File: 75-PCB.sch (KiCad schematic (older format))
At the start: 12 parts

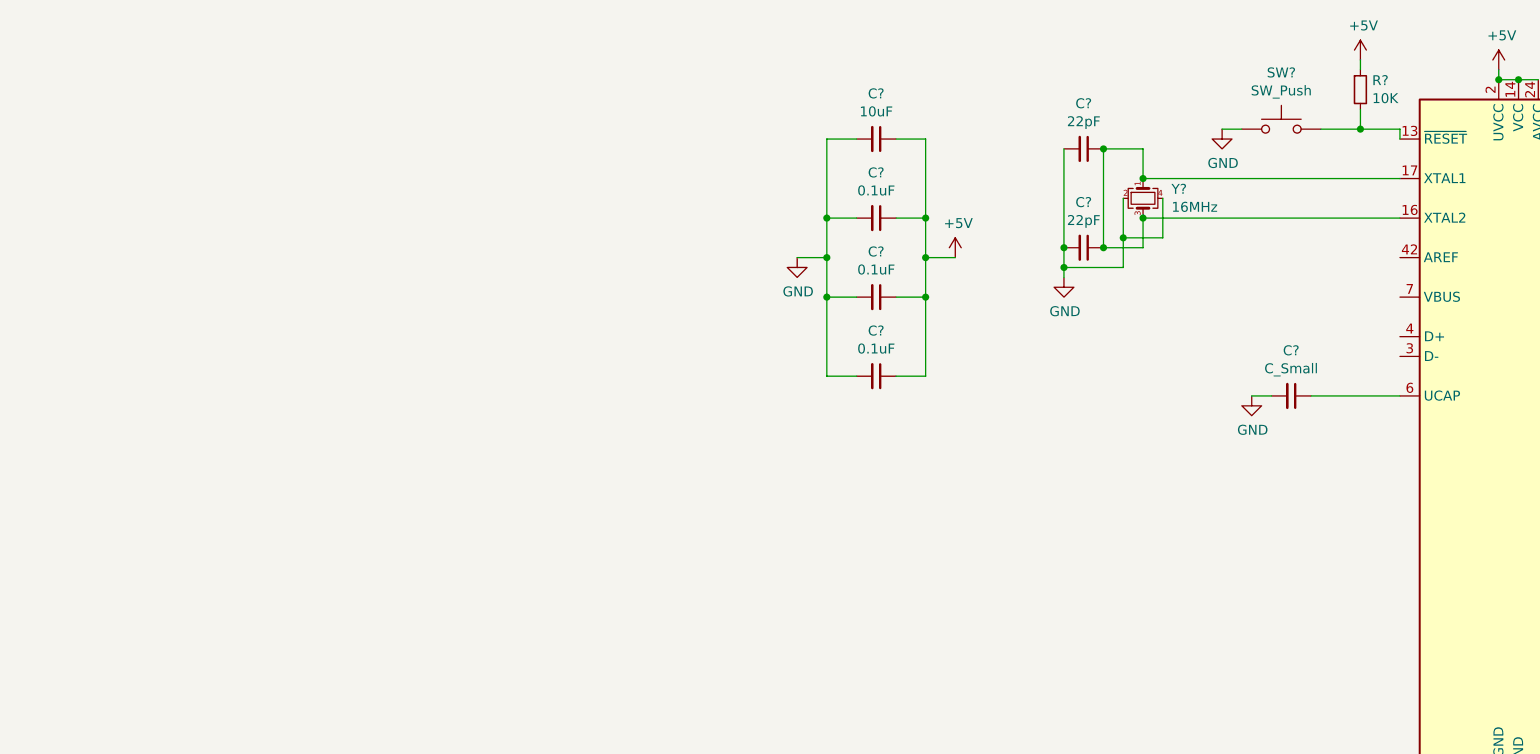
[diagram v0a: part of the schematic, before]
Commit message: Finished USB schematic
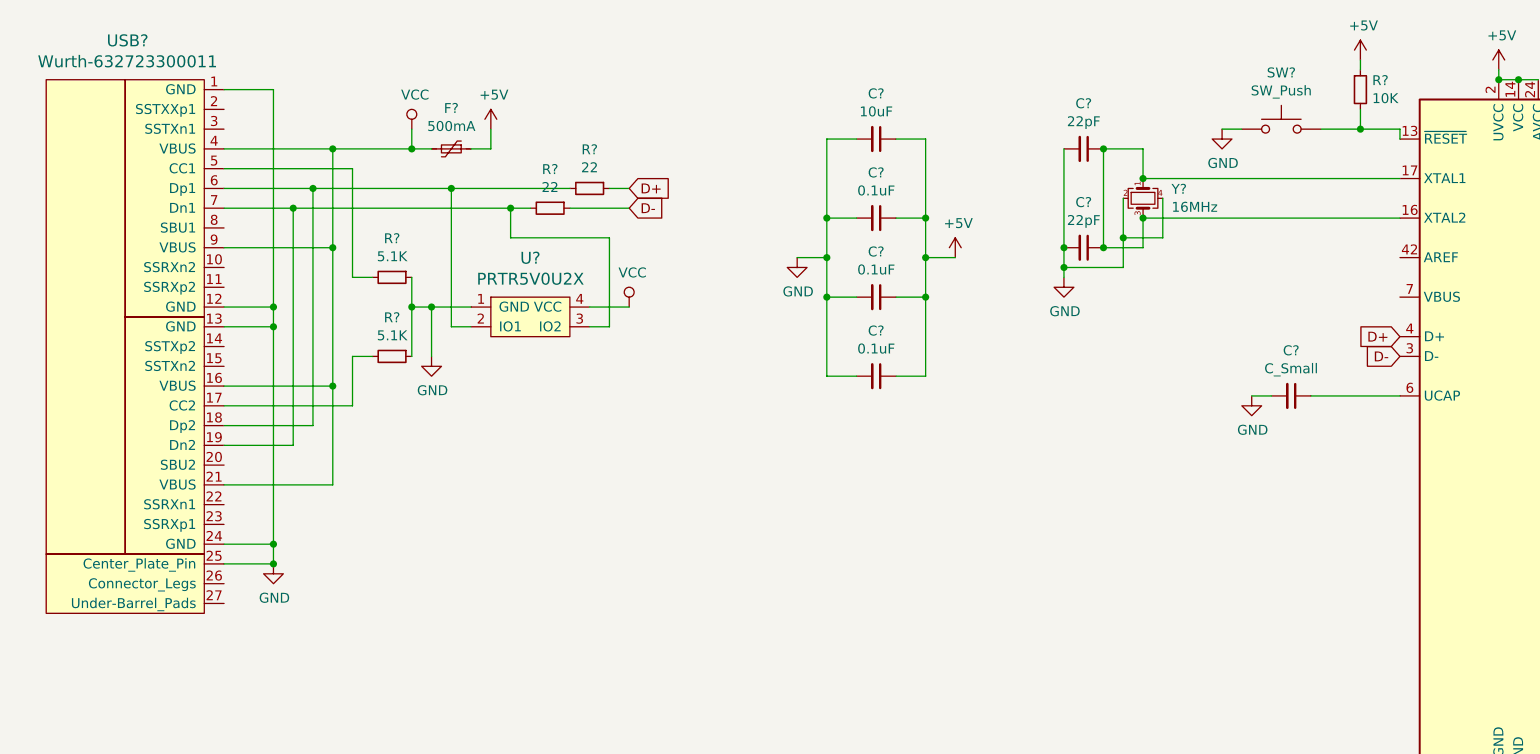
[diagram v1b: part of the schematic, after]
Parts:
- added F?: 500mA, symbol Device:Polyfuse_Small
- added R? (x2): 22, symbol Device:R_Small
- added R? (x2): 5.1K, symbol Device:R_Small
- added U?: PRTR5V0U2X, symbol random-keyboard-parts:PRTR5V0U2X
- added USB?: Wurth-632723300011, symbol Type-C:Wurth-632723300011
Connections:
- net +5V: now also F?.1
- net GND: now also R?.1, R?.1, U?.1 (GND), USB?.1 (GND), USB?.12 (GND), USB?.13 (GND), USB?.24 (GND), USB?.25 (Center_Plate_Pin)
- net D-: now reaches U?.3 (D-)
- net D-: now also R?.1
- net D+: now reaches U?.4 (D+)
- net D+: now also R?.1
- new net: R?.2, USB?.17 (CC2)
- new net: R?.2, U?.2 (IO1), USB?.18 (Dp2), USB?.6 (Dp1)
- new net: R?.2, U?.3 (IO2), USB?.19 (Dn2), USB?.7 (Dn1)
- new net: R?.2, USB?.5 (CC1)
- new net VCC: F?.2, U?.4 (VCC), USB?.16 (VBUS), USB?.21 (VBUS), USB?.4 (VBUS), USB?.9 (VBUS)

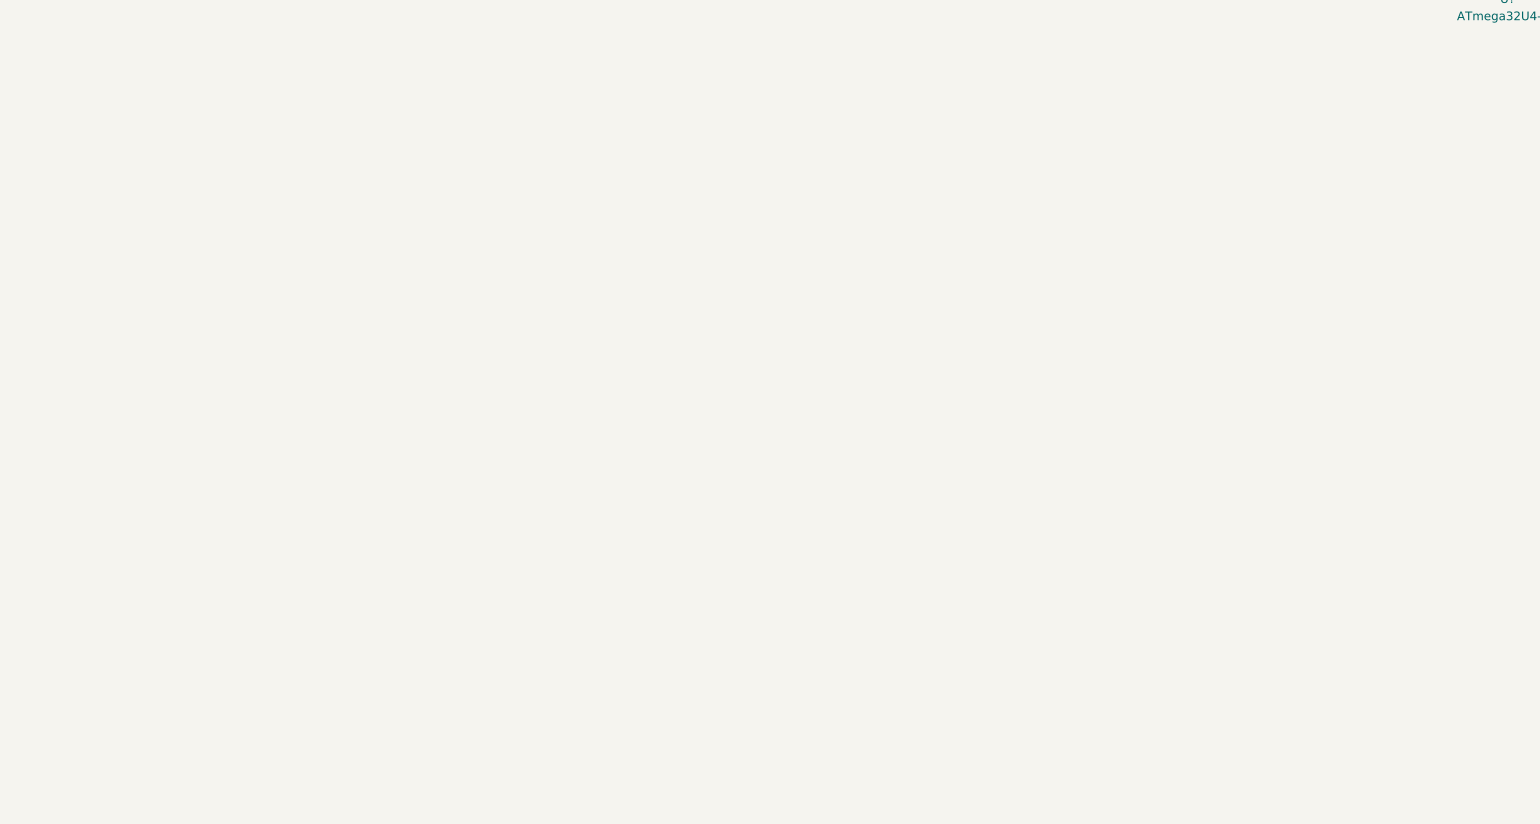
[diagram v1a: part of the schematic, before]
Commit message: Finished placing switch symbols
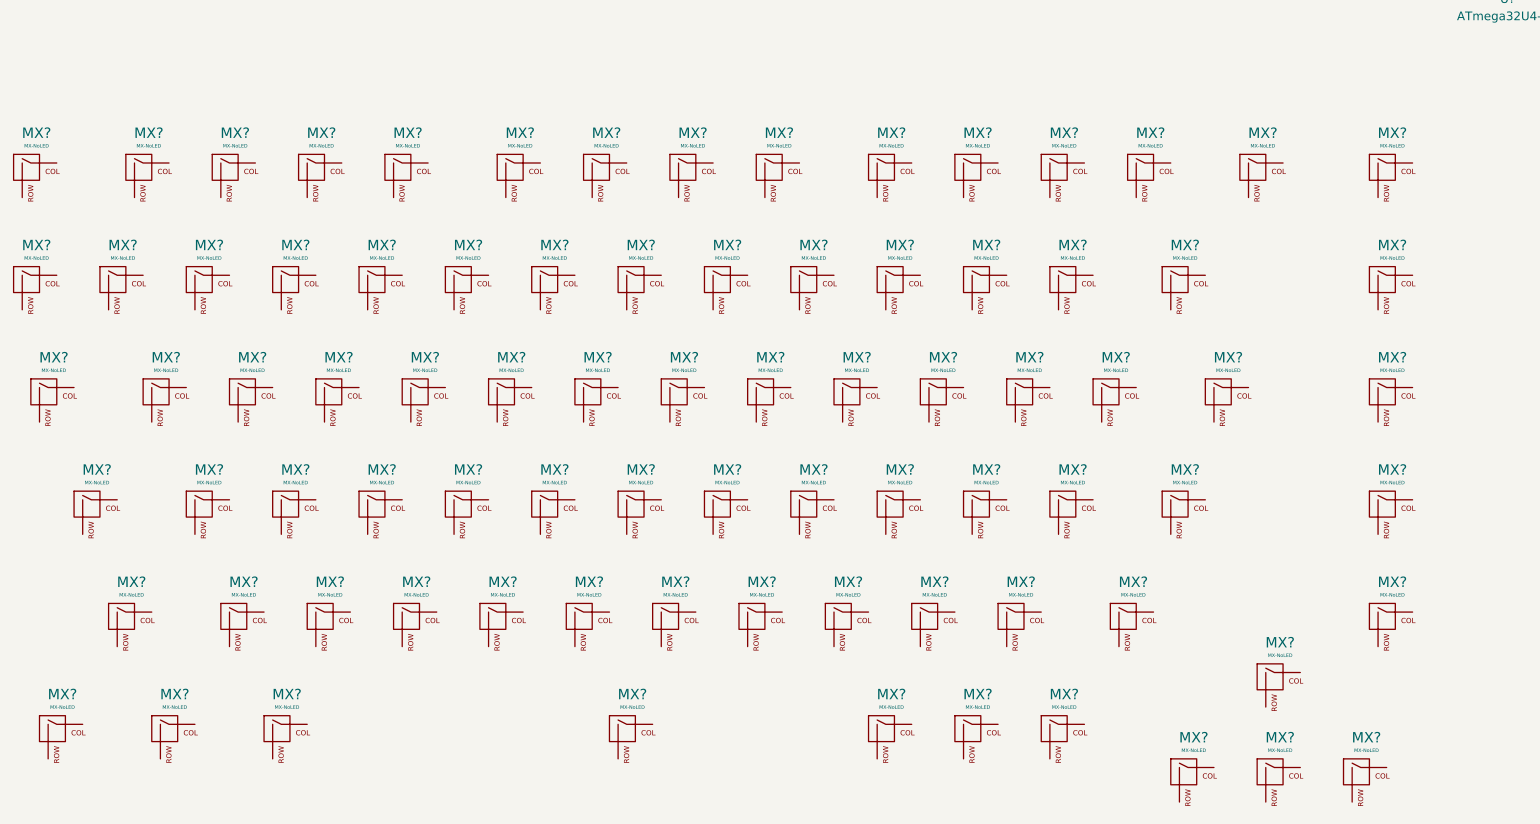
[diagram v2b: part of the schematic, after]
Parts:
- added MX? (x83): MX-NoLED, symbol MX_Alps_Hybrid:MX-NoLED

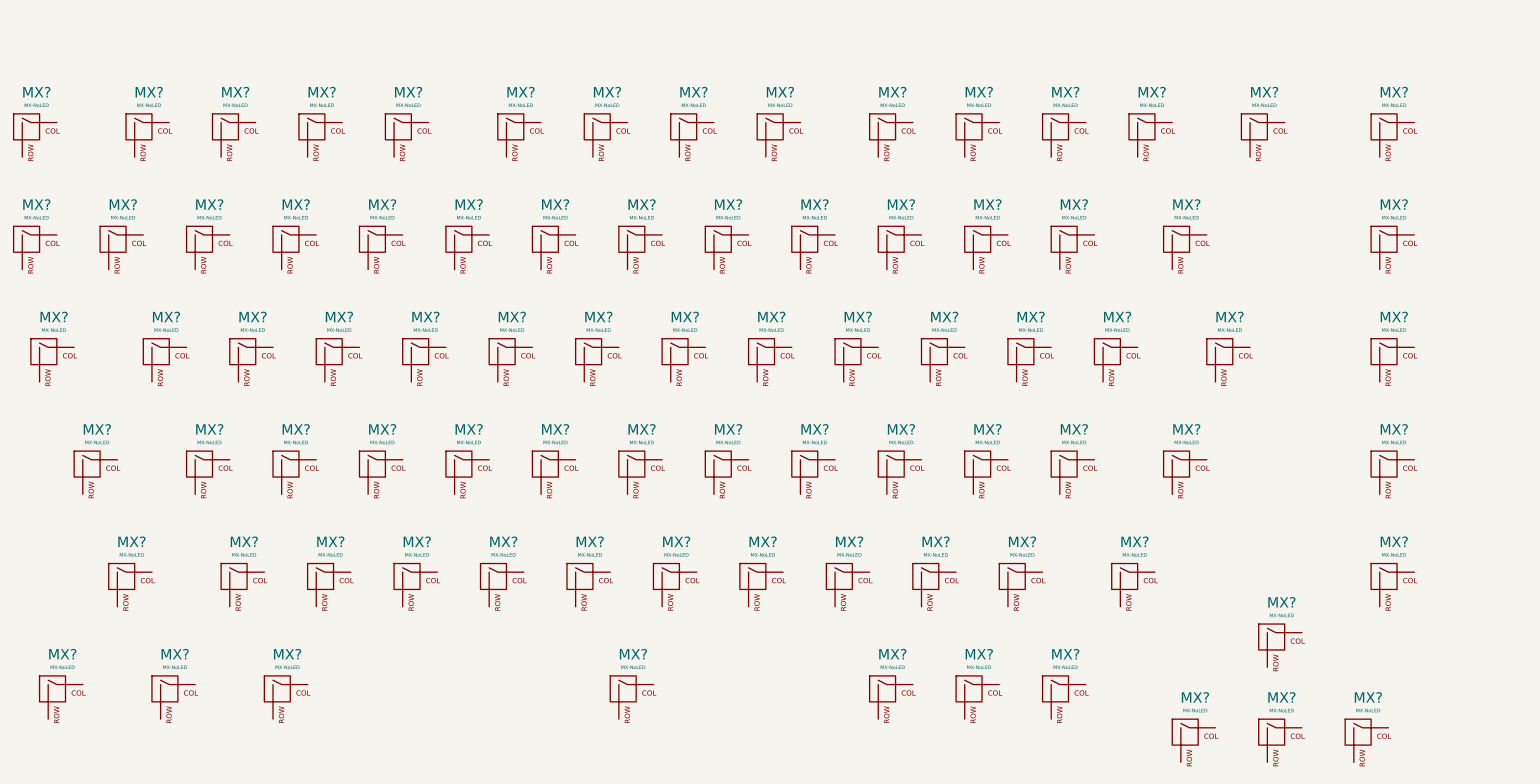
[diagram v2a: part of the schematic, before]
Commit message: Finished columns in switch matrix
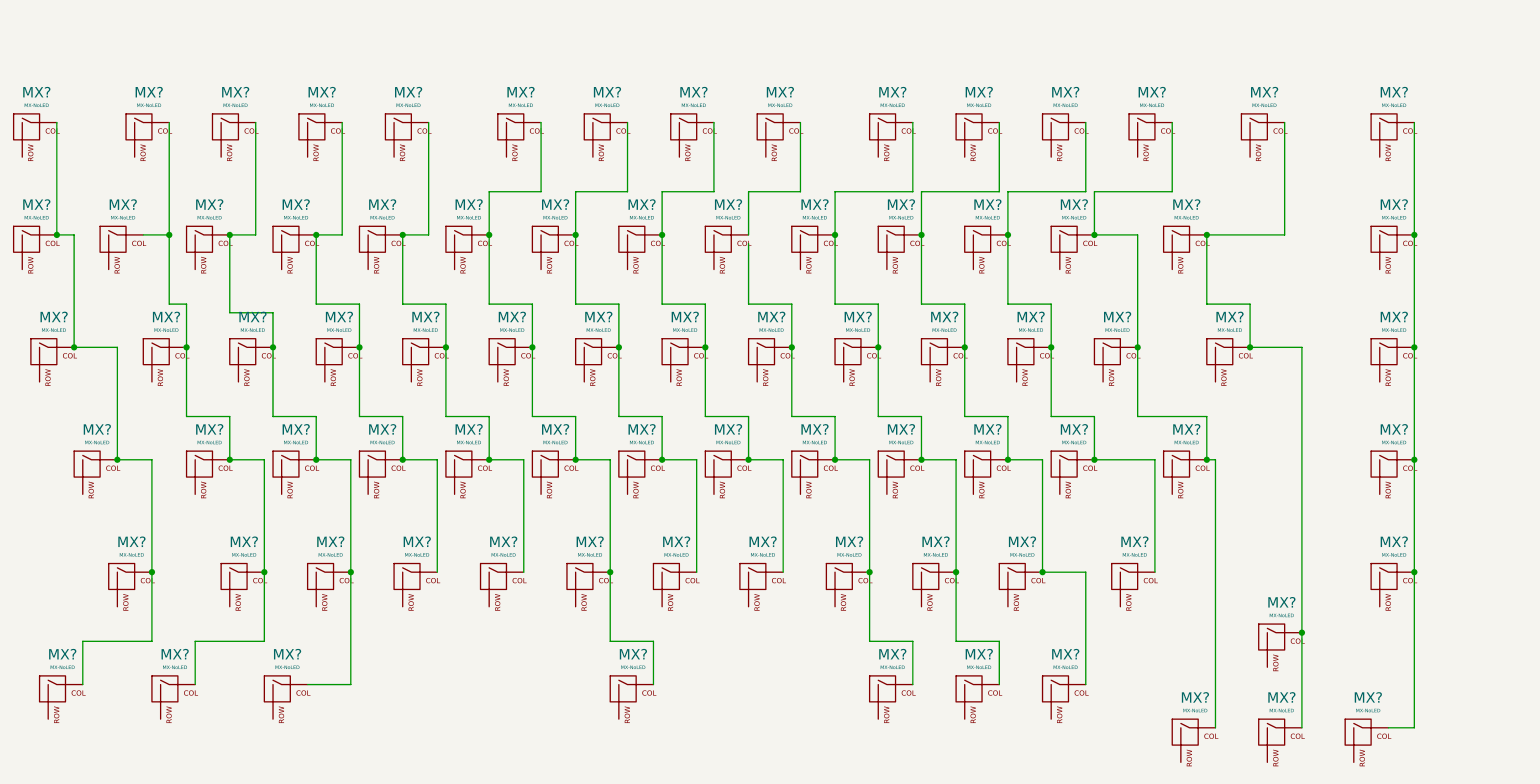
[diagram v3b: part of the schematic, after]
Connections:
- net at MX?.1 (COL): now also MX?.1 (COL), MX?.1 (COL), MX?.1 (COL), MX?.1 (COL), MX?.1 (COL) (x7)
- net at MX?.1 (COL): now also MX?.1 (COL), MX?.1 (COL), MX?.1 (COL), MX?.1 (COL) (x7)
- net at MX?.1 (COL): now also MX?.1 (COL)
- net at MX?.1 (COL): now also MX?.1 (COL), MX?.1 (COL), MX?.1 (COL)

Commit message: Finished switch matrix schematic
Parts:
- added D? (x83): SOD-123, symbol Device:D_Small
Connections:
- net COL0: now reaches MX?.1 (COL), MX?.1 (COL), MX?.1 (COL), MX?.1 (COL), MX?.1 (COL), MX?.1 (COL)
- net at MX?.2 (ROW): now also D?.2 (A) (x82)
- net COL1: now reaches MX?.1 (COL), MX?.1 (COL), MX?.1 (COL), MX?.1 (COL), MX?.1 (COL), MX?.1 (COL)
- net COL2: now reaches MX?.1 (COL), MX?.1 (COL), MX?.1 (COL), MX?.1 (COL), MX?.1 (COL), MX?.1 (COL)
- net COL3: now reaches MX?.1 (COL), MX?.1 (COL), MX?.1 (COL), MX?.1 (COL), MX?.1 (COL)
- net COL4: now reaches MX?.1 (COL), MX?.1 (COL), MX?.1 (COL), MX?.1 (COL), MX?.1 (COL)
- net COL5: now reaches MX?.1 (COL), MX?.1 (COL), MX?.1 (COL), MX?.1 (COL), MX?.1 (COL), MX?.1 (COL)
- net COL6: now reaches MX?.1 (COL), MX?.1 (COL), MX?.1 (COL), MX?.1 (COL), MX?.1 (COL)
- net COL7: now reaches MX?.1 (COL), MX?.1 (COL), MX?.1 (COL), MX?.1 (COL), MX?.1 (COL)
- net COL8: now reaches MX?.1 (COL), MX?.1 (COL)
- net COL8: now also MX?.1 (COL), MX?.1 (COL), MX?.1 (COL), MX?.1 (COL)
- net COL9: now reaches MX?.1 (COL), MX?.1 (COL), MX?.1 (COL), MX?.1 (COL), MX?.1 (COL), MX?.1 (COL)
- net COL10: now reaches MX?.1 (COL), MX?.1 (COL), MX?.1 (COL), MX?.1 (COL), MX?.1 (COL), MX?.1 (COL)
- net COL11: now reaches MX?.1 (COL), MX?.1 (COL), MX?.1 (COL), MX?.1 (COL), MX?.1 (COL)
- net COL12: now reaches MX?.1 (COL), MX?.1 (COL), MX?.1 (COL), MX?.1 (COL), MX?.1 (COL)
- net COL13: now reaches MX?.1 (COL), MX?.1 (COL), MX?.1 (COL), MX?.1 (COL), MX?.1 (COL)
- net COL14: now reaches MX?.1 (COL), MX?.1 (COL), MX?.1 (COL), MX?.1 (COL), MX?.1 (COL), MX?.1 (COL)
- net ROW4: now reaches MX?.2 (ROW)
- net ROW4: now also D?.2 (A)
- new net: D?.1 (K), D?.1 (K), D?.1 (K), D?.1 (K), D?.1 (K), D?.1 (K), D?.1 (K), D?.1 (K), D?.1 (K), D?.1 (K), D?.1 (K), D?.1 (K), D?.1 (K), D?.1 (K)
- new net ROW0: D?.1 (K), D?.1 (K), D?.1 (K), D?.1 (K), D?.1 (K), D?.1 (K), D?.1 (K), D?.1 (K), D?.1 (K), D?.1 (K), D?.1 (K), D?.1 (K), D?.1 (K), D?.1 (K), D?.1 (K)
- new net ROW1: D?.1 (K), D?.1 (K), D?.1 (K), D?.1 (K), D?.1 (K), D?.1 (K), D?.1 (K), D?.1 (K), D?.1 (K), D?.1 (K), D?.1 (K), D?.1 (K), D?.1 (K), D?.1 (K), D?.1 (K)
- new net ROW2: D?.1 (K), D?.1 (K), D?.1 (K), D?.1 (K), D?.1 (K), D?.1 (K), D?.1 (K), D?.1 (K), D?.1 (K), D?.1 (K), D?.1 (K), D?.1 (K), D?.1 (K), D?.1 (K), D?.1 (K)
- new net ROW3: D?.1 (K), D?.1 (K), D?.1 (K), D?.1 (K), D?.1 (K), D?.1 (K), D?.1 (K), D?.1 (K), D?.1 (K), D?.1 (K), D?.1 (K), D?.1 (K), D?.1 (K), D?.1 (K)
- new net ROW5: D?.1 (K), D?.1 (K), D?.1 (K), D?.1 (K), D?.1 (K), D?.1 (K), D?.1 (K), D?.1 (K), D?.1 (K), D?.1 (K)
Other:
- moved on the sheet: C?, F?, MX?, R?, SW?, U?, USB?, Y?

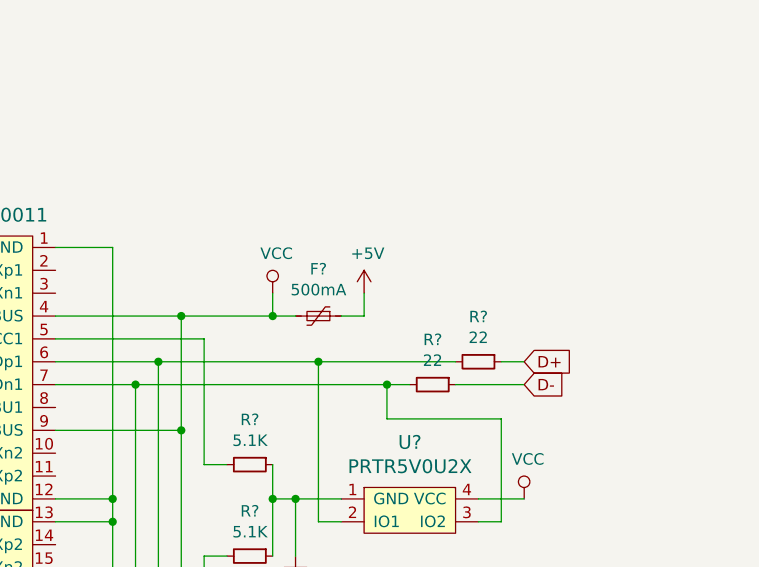
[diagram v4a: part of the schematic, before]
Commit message: Added Schottky diode
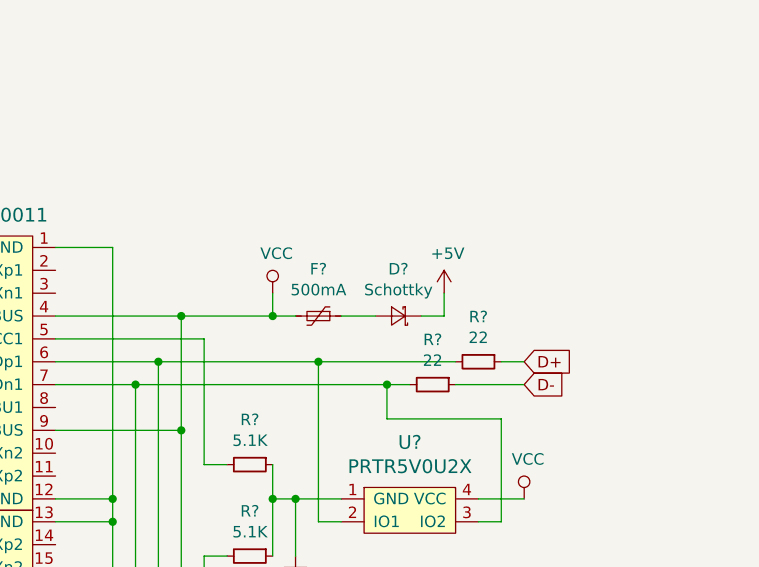
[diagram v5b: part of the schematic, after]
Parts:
- added D?: Schottky, symbol Device:D_Schottky_Small
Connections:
- net +5V: now also D?.1 (K); no longer F?.1
- new net: D?.2 (A), F?.1
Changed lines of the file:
@@
 	0    1    1    0
 $EndComp
-Wire Wire Line
-	14150 6650 14250 6650
 $Comp
 L power:+5V #PWR?
 U 1 1 5E8E2D63
-P 14250 6550
-F 0 "#PWR?" H 14250 6400 50  0001 C CNN
-F 1 "+5V" H 14265 6723 50  0000 C CNN
-F 2 "" H 14250 6550 50  0001 C CNN
-F 3 "" H 14250 6550 50  0001 C CNN
-	1    14250 6550
+P 14600 6550
+F 0 "#PWR?" H 14600 6400 50  0001 C CNN
+F 1 "+5V" H 14615 6723 50  0000 C CNN
+F 2 "" H 14600 6550 50  0001 C CNN
+F 3 "" H 14600 6550 50  0001 C CNN
+	1    14600 6550
 	1    0    0    -1
 $EndComp
@@
 	14650 6950 14950 6950
 Wire Wire Line
-	14250 6650 14250 6550
-Wire Wire Line
 	13450 6650 13850 6650
 Wire Wire Line
@@
 Text GLabel 10150 6350 2    50   Input ~ 0
 ROW5
+$Comp
+L Device:D_Schottky_Small D?
+U 1 1 617B5949
+P 14400 6650
+F 0 "D?" H 14400 6445 50  0000 C CNN
+F 1 "Schottky" H 14400 6536 50  0000 C CNN
+F 2 "" V 14400 6650 50  0001 C CNN
+F 3 "~" V 14400 6650 50  0001 C CNN
+	1    14400 6650
+	-1   0    0    1
+$EndComp
+Wire Wire Line
+	14150 6650 14300 6650
+Wire Wire Line
+	14500 6650 14600 6650
+Wire Wire Line
+	14600 6650 14600 6550
 $EndSCHEMATC
